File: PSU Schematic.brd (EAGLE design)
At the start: 50.3 x 100 mm, 19 parts, among them IC1 LM34, J1 POWERPOLE_POWER45A, J2 FUSEATC, J3 POWERPOLE_POWER45A, J4 FUSEATC

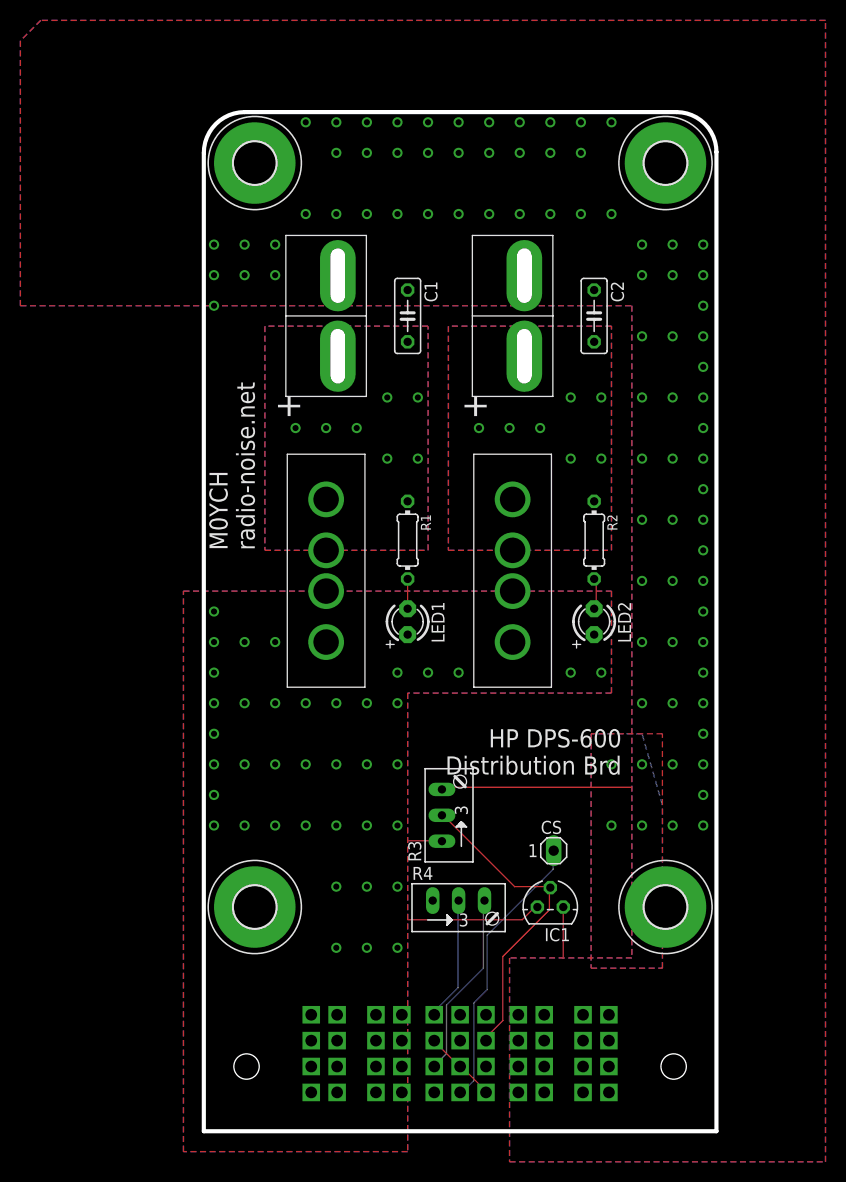
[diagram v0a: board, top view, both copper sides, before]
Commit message: Added voltage decrease. Design Rules Updated.
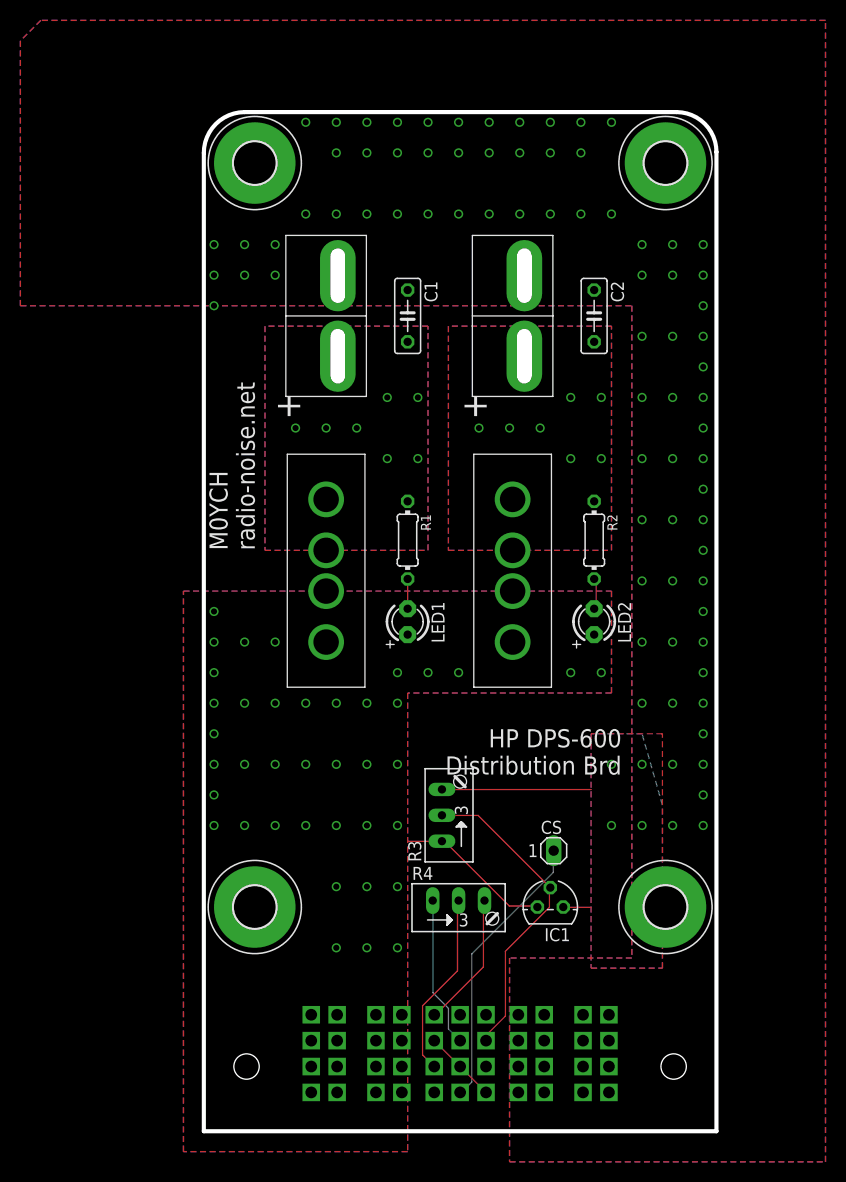
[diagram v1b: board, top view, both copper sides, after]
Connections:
- removed net VCTRL: R4.A, U$2.SIG9
- new net N$1: R4.E, U$2.SIG5
- new net N$2: R4.S, U$2.SIG9
- net 5VCC: now also R4.A; no longer R4.S
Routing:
- net VCTRL: track 18.3 -> 0.00 mm
- net N$2: track 0.00 -> 18.3 mm
- net N$1: track 0.00 -> 14.9 mm
- net GND: track 23.8 -> 17.4 mm
- net LVCC: track 16.6 -> 15.4 mm
- net 5VCC: track 12.2 -> 13.4 mm
